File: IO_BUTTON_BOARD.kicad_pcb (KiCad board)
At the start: 2 copper layers, 80 x 40 mm, 117 parts, among them P1 I2C, P10 IO_7, P2 I2C, P3 IO_0, P4 IO_1, P5 IO_2, P6 IO_3, P7 IO_4, P8 IO_5, P9 IO_6, Q1 NPN, Q10 PNP, Q11 PNP, Q12 PNP, Q13 PNP, Q2 PNP, Q3 NPN, Q4 PNP, Q5 NPN, Q6 PNP, Q7 PNP, Q8 PNP, Q9 PNP, SW1 I2C_ADDR, SW2 SW_0, SW3 SW_1, SW4 SW_2, SW5 SW_3, SW6 SW_4, SW7 SW_5, SW8 SW_6, SW9 SW_7, U1 PCF8574A, U2 74HC86, U3 74HC86

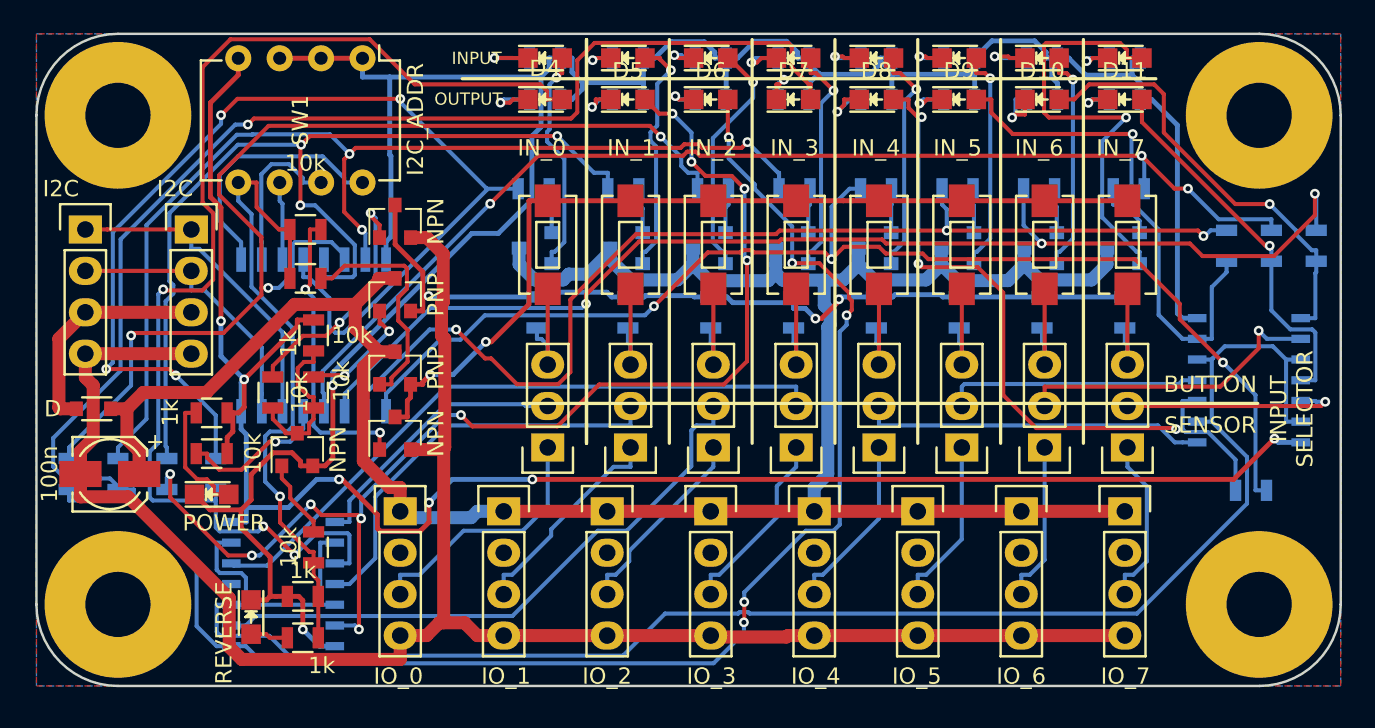
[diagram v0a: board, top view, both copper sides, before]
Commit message: Change positions and orientation of connectors on the pcb
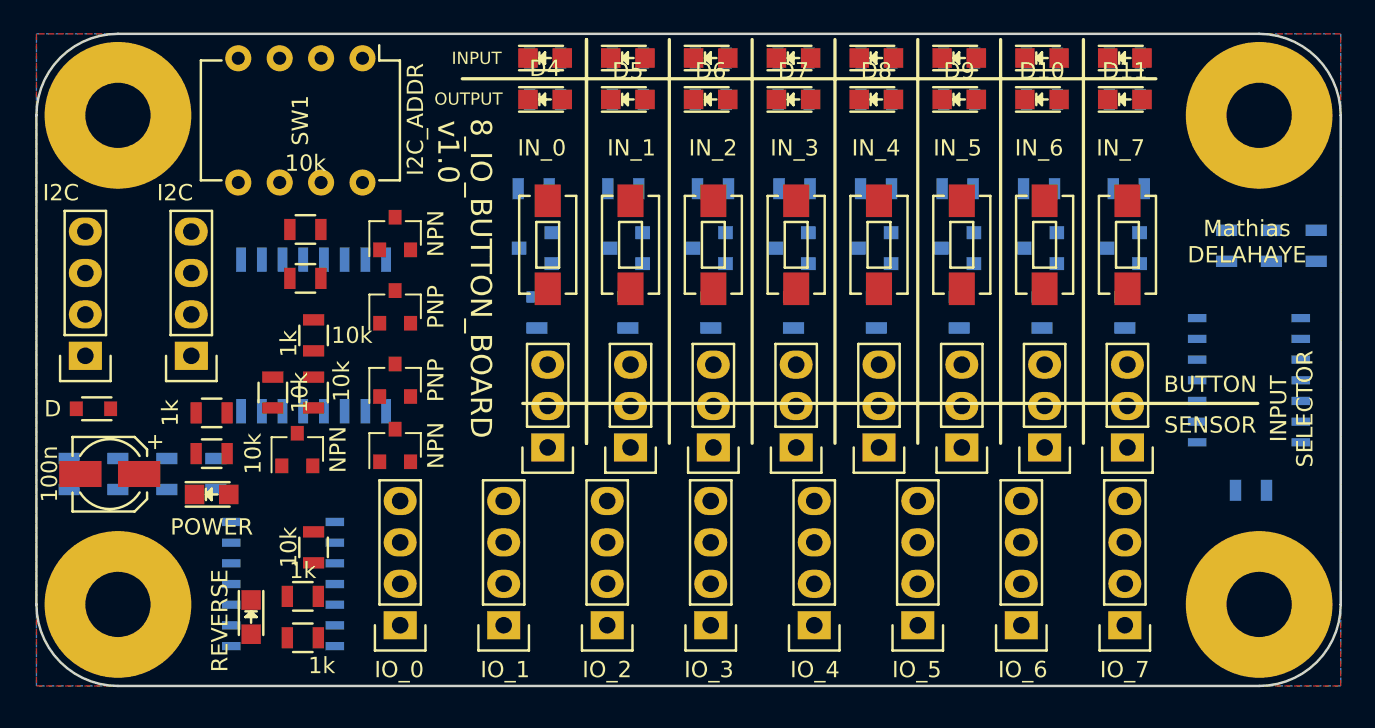
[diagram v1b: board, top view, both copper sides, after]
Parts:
- moved P1 7.75 mm to (109.5, 119.8), turned to 180 degrees
- moved P2 7.75 mm to (103.0, 119.8), turned to 180 degrees
- moved P10 6.99 mm to (166.8, 136.3), turned to 180 degrees
- moved P3 6.99 mm to (122.3, 136.3), turned to 180 degrees
- moved P4 6.99 mm to (128.7, 136.3), turned to 180 degrees
- moved P5 6.99 mm to (135.0, 136.3), turned to 180 degrees
- moved P6 6.99 mm to (141.4, 136.3), turned to 180 degrees
- moved P7 6.99 mm to (147.7, 136.3), turned to 180 degrees
- moved P8 6.99 mm to (154.1, 136.3), turned to 180 degrees
- moved P9 6.99 mm to (160.4, 136.3), turned to 180 degrees
- moved Q2 0.75 mm to (122.0, 121.2)
- moved Q3 0.75 mm to (122.0, 125.2)
- moved Q4 0.75 mm to (122.0, 116.8)
- moved Q5 0.75 mm to (122.0, 112.2)
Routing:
- net GND: track 162.7 -> 0.00 mm, vias 2 -> 0
- net /5V_PWR: track 150.5 -> 0.00 mm
- net /GND_PWR: track 115.2 -> 0.00 mm
- net VCC: track 113.0 -> 0.00 mm, vias 6 -> 0
- net /PULL_LANE_D: track 109.9 -> 0.00 mm
- net Net-(D6-Pad2): track 89.5 -> 0.00 mm, vias 5 -> 0
- net Net-(D7-Pad2): track 82.1 -> 0.00 mm, vias 1 -> 0
- net Net-(R30-Pad1): track 74.9 -> 0.00 mm, vias 3 -> 0
- net Net-(D5-Pad2): track 74.8 -> 0.00 mm, vias 10 -> 0
- net Net-(R28-Pad1): track 73.7 -> 0.00 mm, vias 3 -> 0
- net Net-(D4-Pad2): track 73.2 -> 0.00 mm, vias 3 -> 0
- net Net-(R27-Pad1): track 70.7 -> 0.00 mm, vias 3 -> 0
- net Net-(R34-Pad1): track 68.6 -> 0.00 mm, vias 4 -> 0
- net Net-(R32-Pad1): track 67.6 -> 0.00 mm, vias 3 -> 0
- net Net-(R29-Pad1): track 66.4 -> 0.00 mm, vias 3 -> 0
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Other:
- board text added: "8_IO_BUTTON_BOARD"
- board text added: "Mathias DELAHAYE"
- board text added: "v1.0"

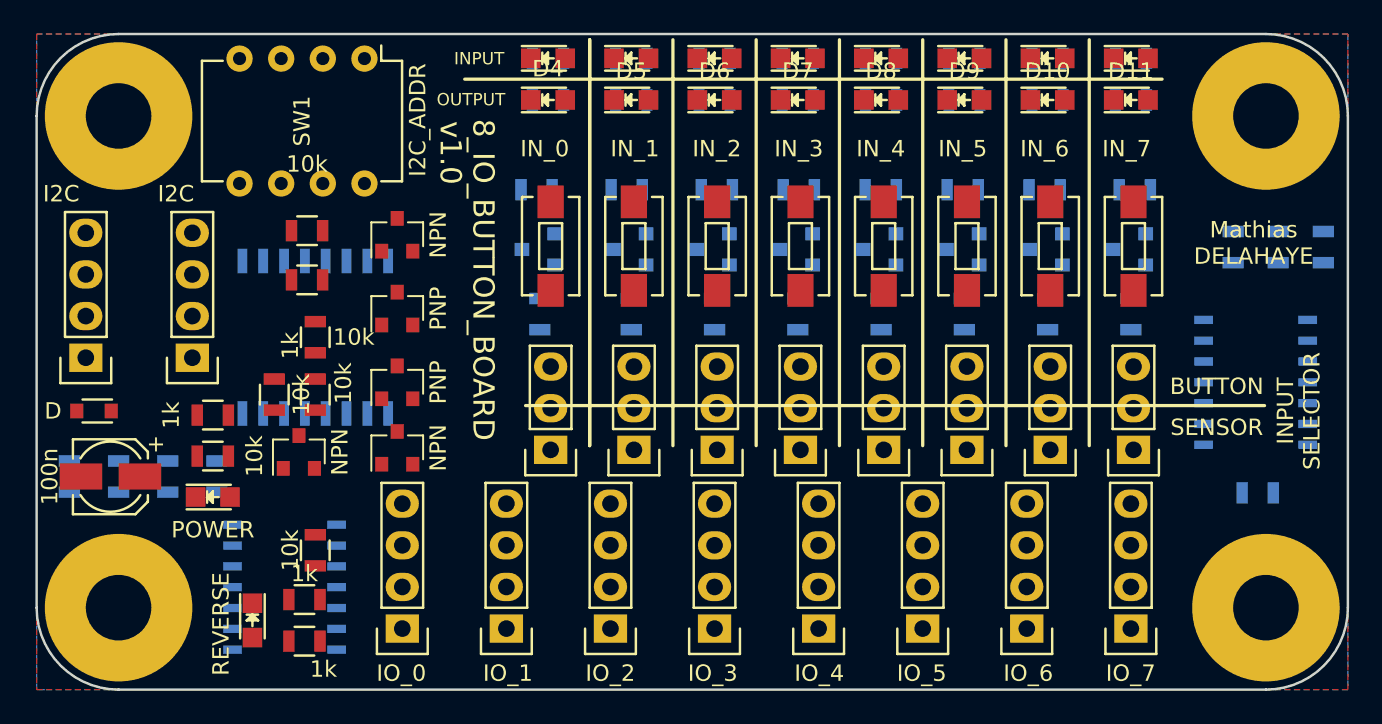
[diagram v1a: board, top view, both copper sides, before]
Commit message: Fix missing pull resistor Reroute PCB
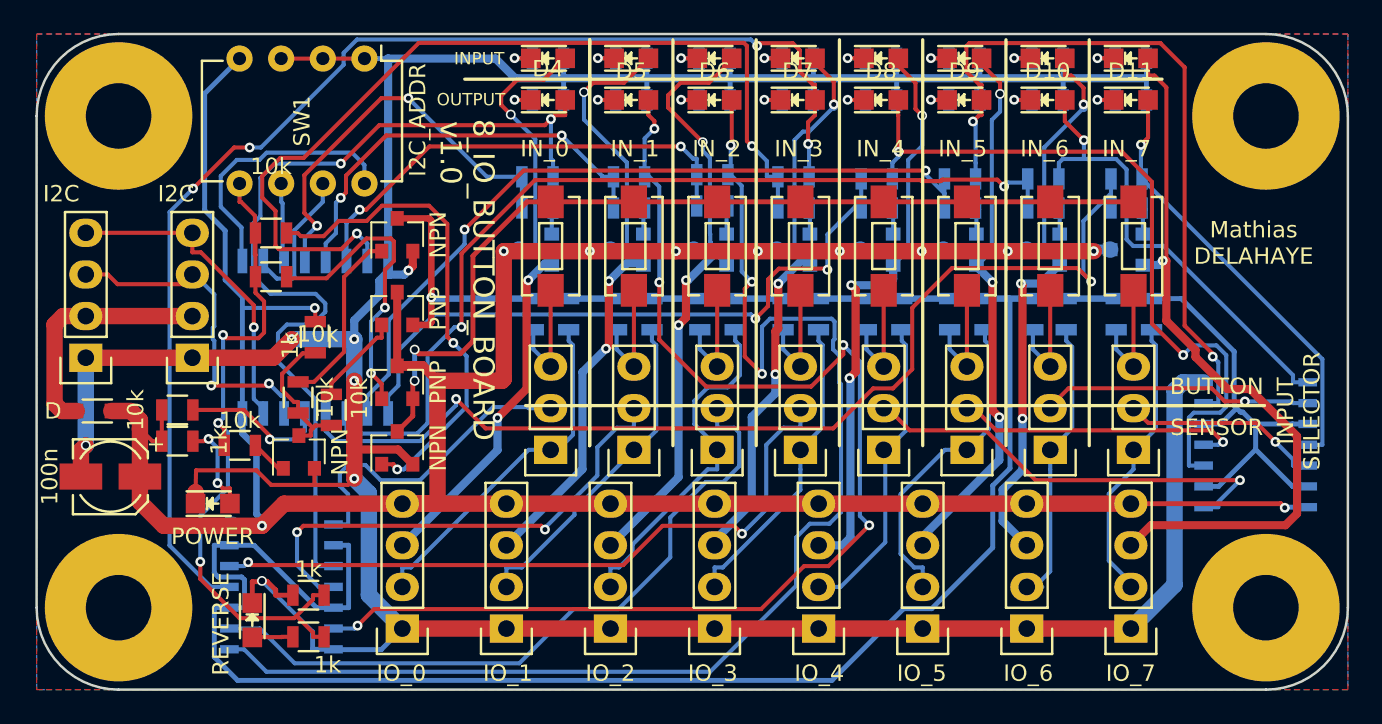
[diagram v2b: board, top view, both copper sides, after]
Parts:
- added R51: 1k, Resistors_SMD:R_0805, B.Cu at (132.5, 117.1)
- added R52: 1k, Resistors_SMD:R_0805, B.Cu at (137.5, 117.1)
- added R53: 1k, Resistors_SMD:R_0805, B.Cu at (142.6, 117.1)
- added R54: 1k, Resistors_SMD:R_0805, B.Cu at (147.7, 117.1)
- added R55: 1k, Resistors_SMD:R_0805, B.Cu at (152.8, 117.1)
- added R56: 1k, Resistors_SMD:R_0805, B.Cu at (157.9, 117.1)
- added R57: 1k, Resistors_SMD:R_0805, B.Cu at (162.8, 117.1)
- added R58: 1k, Resistors_SMD:R_0805, B.Cu at (168.0, 117.1)
- moved R31 45.1 mm to (146.2, 108.7), turned to 0 degrees
- moved R32 43.3 mm to (141.2, 108.6), turned to 0 degrees
- moved R33 33.6 mm to (136.1, 108.7), turned to 0 degrees
- moved R30 30.1 mm to (151.3, 108.8), turned to 0 degrees
- moved R34 26.8 mm to (130.6, 108.7), turned to 0 degrees
- moved R28 17.6 mm to (161.4, 108.8), turned to 0 degrees
- moved R29 17.2 mm to (156.3, 108.8), turned to 0 degrees
- moved R27 10.1 mm to (166.5, 108.8), turned to 0 degrees
- moved R2 7.89 mm to (112.4, 125.1), turned to 180 degrees
- moved U3 3.81 mm to (174.5, 125.1)
- moved R10 3.55 mm to (108.6, 122.9), turned to 180 degrees
- moved R7 2.69 mm to (108.6, 124.8), turned to 0 degrees
- moved R5 2.21 mm to (114.3, 114.8)
- moved R6 2.20 mm to (114.3, 112.1)
- moved R9 1.46 mm to (116.0, 122.2)
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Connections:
- C1 pad 1: /5V_PWR -> VCC
- C1 pad 2: /GND_PWR -> GND
- D12 pad 2: /D_OUT_0 -> /OUT_0
- D13 pad 2: /D_OUT_1 -> /OUT_1
- D14 pad 2: /D_OUT_2 -> /OUT_2
- D15 pad 2: /D_OUT_3 -> /OUT_3
- D16 pad 2: /D_OUT_4 -> /OUT_4
- D17 pad 2: /D_OUT_5 -> /OUT_5
- D18 pad 2: /D_OUT_6 -> /OUT_6
- D19 pad 2: /D_OUT_7 -> /OUT_7
- D2 pad 1: /5V_PWR -> VCC
- P1 pad 1: /SCL -> GND
- P1 pad 2: /SDA -> Net-(D2-Pad2)
- P1 pad 3: Net-(D2-Pad2) -> /SCL
- P1 pad 4: /GND_PWR -> /SDA
- P10 pad 1: /5V_PWR -> GND
- P10 pad 2: /OUT_7 -> /IN_7
- P10 pad 3: /IN_7 -> /OUT_7
- P10 pad 4: /GND_PWR -> VCC
- P2 pad 1: /SCL -> GND
- P2 pad 2: /SDA -> Net-(D2-Pad2)
- P2 pad 3: Net-(D2-Pad2) -> /SCL
- P2 pad 4: /GND_PWR -> /SDA
- P3 pad 1: /5V_PWR -> GND
- P3 pad 2: /OUT_0 -> /IN_0
- P3 pad 3: /IN_0 -> /OUT_0
- P3 pad 4: /GND_PWR -> VCC
- P4 pad 1: /5V_PWR -> GND
- P4 pad 2: /OUT_1 -> /IN_1
- P4 pad 3: /IN_1 -> /OUT_1
- P4 pad 4: /GND_PWR -> VCC
- P5 pad 1: /5V_PWR -> GND
- P5 pad 2: /OUT_2 -> /IN_2
- P5 pad 3: /IN_2 -> /OUT_2
- P5 pad 4: /GND_PWR -> VCC
- P6 pad 1: /5V_PWR -> GND
- P6 pad 2: /OUT_3 -> /IN_3
- P6 pad 3: /IN_3 -> /OUT_3
- P6 pad 4: /GND_PWR -> VCC
- P7 pad 1: /5V_PWR -> GND
- P7 pad 2: /OUT_4 -> /IN_4
- P7 pad 3: /IN_4 -> /OUT_4
- P7 pad 4: /GND_PWR -> VCC
- P8 pad 1: /5V_PWR -> GND
- P8 pad 2: /OUT_5 -> /IN_5
- P8 pad 3: /IN_5 -> /OUT_5
- P8 pad 4: /GND_PWR -> VCC
- P9 pad 1: /5V_PWR -> GND
- P9 pad 2: /OUT_6 -> /IN_6
- P9 pad 3: /IN_6 -> /OUT_6
- P9 pad 4: /GND_PWR -> VCC
- Q10 pad 2: /D_OUT_4 -> /OUT_4
- Q10 pad 3: /5V_PWR -> VCC
- Q11 pad 2: /D_OUT_5 -> /OUT_5
- Q11 pad 3: /5V_PWR -> VCC
- Q12 pad 2: /D_OUT_6 -> /OUT_6
- Q12 pad 3: /5V_PWR -> VCC
- Q13 pad 2: /D_OUT_7 -> /OUT_7
- Q13 pad 3: /5V_PWR -> VCC
- Q2 pad 3: /5V_PWR -> VCC
- Q3 pad 2: /GND_PWR -> GND
- Q4 pad 3: /5V_PWR -> VCC
- Q5 pad 2: /GND_PWR -> GND
- Q6 pad 2: /D_OUT_0 -> /OUT_0
- Q6 pad 3: /5V_PWR -> VCC
- Q7 pad 2: /D_OUT_1 -> /OUT_1
- Q7 pad 3: /5V_PWR -> VCC
- Q8 pad 2: /D_OUT_2 -> /OUT_2
- Q8 pad 3: /5V_PWR -> VCC
- Q9 pad 2: /D_OUT_3 -> /OUT_3
- Q9 pad 3: /5V_PWR -> VCC
- U2 pad 10: /PULL_LANE_D -> /PULL_LANE
- U2 pad 13: /PULL_LANE_D -> /PULL_LANE
- U2 pad 2: /PULL_LANE_D -> /PULL_LANE
- U2 pad 5: /PULL_LANE_D -> /PULL_LANE
- U3 pad 10: /PULL_LANE_D -> /PULL_LANE
- U3 pad 13: /PULL_LANE_D -> /PULL_LANE
- U3 pad 2: /PULL_LANE_D -> /PULL_LANE
- U3 pad 5: /PULL_LANE_D -> /PULL_LANE
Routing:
- net GND: track 0.00 -> 233.5 mm, vias 0 -> 7
- net VCC: track 0.00 -> 197.1 mm, vias 0 -> 11
- net /PULL_LANE: track 0.00 -> 172.2 mm, vias 0 -> 1
- net Net-(D6-Pad2): track 0.00 -> 81.1 mm, vias 0 -> 3
- net Net-(D7-Pad2): track 0.00 -> 77.1 mm, vias 0 -> 4
- net Net-(D5-Pad2): track 0.00 -> 76.4 mm, vias 0 -> 5
- net Net-(R27-Pad1): track 0.00 -> 64.7 mm, vias 0 -> 2
- net Net-(R28-Pad1): track 0.00 -> 56.3 mm, vias 0 -> 2
- net /CONTACT_LANE: track 0.00 -> 56.3 mm, vias 0 -> 2
- net Net-(R31-Pad1): track 0.00 -> 56.1 mm, vias 0 -> 2
- net Net-(D4-Pad2): track 0.00 -> 56.0 mm, vias 0 -> 2
- net Net-(R29-Pad1): track 0.00 -> 47.0 mm, vias 0 -> 2
- net Net-(D9-Pad2): track 0.00 -> 46.1 mm, vias 0 -> 2
- net /OUT_7: track 0.00 -> 45.8 mm, vias 0 -> 1
- net Net-(D8-Pad2): track 0.00 -> 45.2 mm, vias 0 -> 2
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- added copper zone on B.Cu, net (none)
- added copper zone on F.Cu, net (none)
- removed copper zone on B.Cu, net /GND_PWR
- removed copper zone on F.Cu, net /GND_PWR
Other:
- net class power_track: trace_width 0.8 -> 1

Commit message: Change marking
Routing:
- added copper zone on B.Cu, net GND
- added copper zone on F.Cu, net GND
- removed copper zone on B.Cu, net (none)
- removed copper zone on F.Cu, net (none)
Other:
- board text added: "Mathias DELAHAYE 2019"
- board text removed: "Mathias DELAHAYE"
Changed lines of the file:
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@@
     (links 235)
     (no_connects 0)
-    (area 99.924999 99.924999 180.075001 140.075001)
+    (area 95.442857 97.525 184.557143 142.575)
     (thickness 1.6)
-    (drawings 26)
+    (drawings 27)
     (tracks 1340)
     (zones 0)
@@
   )
   (page A4)
+  (title_block
+    (title 8_IO_BUTTON_BOARD)
+    (date 2019-03-06)
+    (rev v1.0)
+    (company "Mathias DELAHAYE")
+  )
   (layers
     (0 F.Cu signal)
@@
     (34 B.Paste user)
     (35 F.Paste user)
-    (36 B.SilkS user hide)
-    (37 F.SilkS user hide)
+    (36 B.SilkS user)
+    (37 F.SilkS user)
     (38 B.Mask user)
     (39 F.Mask user)
@@
     (44 Edge.Cuts user)
     (45 Margin user)
-    (46 B.CrtYd user hide)
-    (47 F.CrtYd user hide)
-    (48 B.Fab user hide)
-    (49 F.Fab user hide)
+    (46 B.CrtYd user)
+    (47 F.CrtYd user)
+    (48 B.Fab user)
+    (49 F.Fab user)
   )
   (setup
@@
     (pad_to_mask_clearance 0.2)
     (aux_axis_origin 103 94)
-    (visible_elements FFFFFF0D)
+    (visible_elements FFFFFFFF)
     (pcbplotparams
       (layerselection 0x00030_80000001)
@@
       (drillshape 0)
       (scaleselection 1)
-      (outputdirectory ""))
+      (outputdirectory ../../../tmp/8_IO_BUTTON_BOARD.wiki/img/))
   )
   (net 0 "")
@@
     )
   )
-  (gr_text v1.0 (at 125.25 107.25 270) (layer F.SilkS)
+  (gr_text "Mathias\nDELAHAYE\n2019" (at 175.895 112.268) (layer B.Cu)
+    (effects (font (size 1 1) (thickness 0.25)) (justify mirror))
+  )
+  (gr_text "Mathias\nDELAHAYE\n2019" (at 174.752 115.189) (layer F.Cu)
+    (effects (font (size 1 1) (thickness 0.25)))
+  )
+  (gr_text v1.0 (at 124.841 107.188 270) (layer F.SilkS)
     (effects (font (size 1.3 1.3) (thickness 0.3)))
   )
@@
     (effects (font (size 1.3 1.3) (thickness 0.3)))
   )
-  (gr_text "Mathias\nDELAHAYE" (at 174.25 112.75) (layer F.SilkS)
-    (effects (font (size 1 1) (thickness 0.25)))
-  )
   (gr_text OUTPUT (at 126.5 104) (layer F.SilkS)
     (effects (font (size 0.75 0.75) (thickness 0.1875)))
@@
   (segment (start 155.325 113.145) (end 155.505 113.145) (width 0.6) (layer B.Cu) (net 92))
   (segment (start 155.325 113.145) (end 155.337 113.157) (width 1) (layer B.Cu) (net 92))
-  (zone (net 0) (net_name "") (layer B.Cu) (hatch edge 0.508)
+  (zone (net 1) (net_name GND) (layer B.Cu) (hatch edge 0.508)
     (connect_pads (clearance 0.508))
     (min_thickness 0.254)
@@
     )
   )
-  (zone (net 0) (net_name "") (layer F.Cu) (hatch edge 0.508)
+  (zone (net 1) (net_name GND) (layer F.Cu) (hatch edge 0.508)
     (connect_pads (clearance 0.508))
     (min_thickness 0.254)
